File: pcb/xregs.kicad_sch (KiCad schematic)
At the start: 13 parts

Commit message: WIP schematic
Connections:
- net XD.0: now reaches U?.10 (Q5)
- net XE.0: now reaches U?.11 (Q6)
- net XF.0: now reaches U?.12 (Q7)
- net X8.0: now reaches U?.4 (Q0)
- net X9.0: now reaches U?.5 (Q1)
- net XA.0: now reaches U?.6 (Q2)
- net XB.0: now reaches U?.7 (Q3)
- net XC.0: now reaches U?.9 (Q4)
- net XD.1: now reaches U?.10 (Q5)
- net XE.1: now reaches U?.11 (Q6)
- net XF.1: now reaches U?.12 (Q7)
- net X8.1: now reaches U?.4 (Q0)
- net X9.1: now reaches U?.5 (Q1)
- net XA.1: now reaches U?.6 (Q2)
- net XB.1: now reaches U?.7 (Q3)
- net XC.1: now reaches U?.9 (Q4)

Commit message: WIP schematic
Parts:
- gave numbers to parts that had none: 9
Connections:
- net VCC renamed +5V

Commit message: WIP PCB
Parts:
- renumbered U42 to U?, U46 to U?, U50 to U?, U48 to U?, U47 to U?, U44 to U?, U43 to U?, U45 to U?, U49 to U?
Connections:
- net XD.2: now reaches U?.10 (Q5)
- net XE.2: now reaches U?.11 (Q6)
- net XF.2: now reaches U?.12 (Q7)
- net X8.2: now reaches U?.4 (Q0)
- net X9.2: now reaches U?.5 (Q1)
- net XA.2: now reaches U?.6 (Q2)
- net XB.2: now reaches U?.7 (Q3)
- net XC.2: now reaches U?.9 (Q4)
- net XD.3: now reaches U?.10 (Q5)
- net XE.3: now reaches U?.11 (Q6)
- net XF.3: now reaches U?.12 (Q7)
- net X8.3: now reaches U?.4 (Q0)
- net X9.3: now reaches U?.5 (Q1)
- net XA.3: now reaches U?.6 (Q2)
- net XB.3: now reaches U?.7 (Q3)
- net XC.3: now reaches U?.9 (Q4)

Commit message: PCB: add reset circuit, xtal
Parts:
- gave numbers to parts that had none: 10

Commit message: WIP schematic
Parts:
- renumbered U47 to U48, U48 to U49, U49 to U50, U50 to U51, U51 to U52, U52 to U53, U53 to U54, U54 to U55, U55 to U56, U5 to U6

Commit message: WIP schematic
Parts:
- renumbered U6 to U7
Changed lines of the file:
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@@
 		(dnp no)
 		(fields_autoplaced yes)
-		(property "Reference" "U6"
+		(property "Reference" "U7"
 			(at 62.23 120.6499 0)
 			(effects
@@
 			(project ""
 				(path "/e63e39d7-6ac0-4ffd-8aa3-1841a4541b55/ec11039d-e120-4fa7-aaf4-831995f0a346"
-					(reference "U6")
+					(reference "U7")
 					(unit 5)
 				)

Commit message: WIP schematic
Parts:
- renumbered U7 to U48
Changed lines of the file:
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@@
 		(dnp no)
 		(fields_autoplaced yes)
-		(property "Reference" "#PWR0191"
+		(property "Reference" "#PWR0208"
 			(at 147.32 74.93 0)
 			(effects
@@
 			(project ""
 				(path "/e63e39d7-6ac0-4ffd-8aa3-1841a4541b55/ec11039d-e120-4fa7-aaf4-831995f0a346"
-					(reference "#PWR0191")
+					(reference "#PWR0208")
 					(unit 1)
 				)
@@
 		(dnp no)
 		(fields_autoplaced yes)
-		(property "Reference" "#PWR0195"
+		(property "Reference" "#PWR0212"
 			(at 198.12 74.93 0)
 			(effects
@@
 			(project "fnx51"
 				(path "/e63e39d7-6ac0-4ffd-8aa3-1841a4541b55/ec11039d-e120-4fa7-aaf4-831995f0a346"
-					(reference "#PWR0195")
+					(reference "#PWR0212")
 					(unit 1)
 				)
@@
 		(dnp no)
 		(fields_autoplaced yes)
-		(property "Reference" "#PWR0193"
+		(property "Reference" "#PWR0210"
 			(at 147.32 151.13 0)
 			(effects
@@
 			(project "fnx51"
 				(path "/e63e39d7-6ac0-4ffd-8aa3-1841a4541b55/ec11039d-e120-4fa7-aaf4-831995f0a346"
-					(reference "#PWR0193")
+					(reference "#PWR0210")
 					(unit 1)
 				)
@@
 		(dnp no)
 		(fields_autoplaced yes)
-		(property "Reference" "#PWR0185"
+		(property "Reference" "#PWR0202"
 			(at 55.88 140.97 0)
 			(effects
@@
 			(project ""
 				(path "/e63e39d7-6ac0-4ffd-8aa3-1841a4541b55/ec11039d-e120-4fa7-aaf4-831995f0a346"
-					(reference "#PWR0185")
+					(reference "#PWR0202")
 					(unit 1)
 				)
@@
 		(dnp no)
 		(fields_autoplaced yes)
-		(property "Reference" "#PWR0199"
+		(property "Reference" "#PWR0216"
 			(at 248.92 74.93 0)
 			(effects
@@
 			(project "fnx51"
 				(path "/e63e39d7-6ac0-4ffd-8aa3-1841a4541b55/ec11039d-e120-4fa7-aaf4-831995f0a346"
-					(reference "#PWR0199")
+					(reference "#PWR0216")
 					(unit 1)
 				)
@@
 		(on_board yes)
 		(dnp no)
-		(property "Reference" "#PWR0194"
+		(property "Reference" "#PWR0211"
 			(at 198.12 36.83 0)
 			(effects
@@
 			(project "fnx51"
 				(path "/e63e39d7-6ac0-4ffd-8aa3-1841a4541b55/ec11039d-e120-4fa7-aaf4-831995f0a346"
-					(reference "#PWR0194")
+					(reference "#PWR0211")
 					(unit 1)
 				)
@@
 		(on_board yes)
 		(dnp no)
-		(property "Reference" "#PWR0192"
+		(property "Reference" "#PWR0209"
 			(at 147.32 113.03 0)
 			(effects
@@
 			(project "fnx51"
 				(path "/e63e39d7-6ac0-4ffd-8aa3-1841a4541b55/ec11039d-e120-4fa7-aaf4-831995f0a346"
-					(reference "#PWR0192")
+					(reference "#PWR0209")
 					(unit 1)
 				)
@@
 		(dnp no)
 		(fields_autoplaced yes)
-		(property "Reference" "#PWR0189"
+		(property "Reference" "#PWR0206"
 			(at 96.52 151.13 0)
 			(effects
@@
 			(project "fnx51"
 				(path "/e63e39d7-6ac0-4ffd-8aa3-1841a4541b55/ec11039d-e120-4fa7-aaf4-831995f0a346"
-					(reference "#PWR0189")
+					(reference "#PWR0206")
 					(unit 1)
 				)
@@
 		(dnp no)
 		(fields_autoplaced yes)
-		(property "Reference" "#PWR0187"
+		(property "Reference" "#PWR0204"
 			(at 96.52 74.93 0)
 			(effects
@@
 			(project "fnx51"
 				(path "/e63e39d7-6ac0-4ffd-8aa3-1841a4541b55/ec11039d-e120-4fa7-aaf4-831995f0a346"
-					(reference "#PWR0187")
+					(reference "#PWR0204")
 					(unit 1)
 				)
@@
 		(on_board yes)
 		(dnp no)
-		(property "Reference" "#PWR0200"
+		(property "Reference" "#PWR0217"
 			(at 248.92 113.03 0)
 			(effects
@@
 			(project "fnx51"
 				(path "/e63e39d7-6ac0-4ffd-8aa3-1841a4541b55/ec11039d-e120-4fa7-aaf4-831995f0a346"
-					(reference "#PWR0200")
+					(reference "#PWR0217")
 					(unit 1)
 				)
@@
 		(dnp no)
 		(fields_autoplaced yes)
-		(property "Reference" "#PWR0197"
+		(property "Reference" "#PWR0214"
 			(at 198.12 151.13 0)
 			(effects
@@
 			(project "fnx51"
 				(path "/e63e39d7-6ac0-4ffd-8aa3-1841a4541b55/ec11039d-e120-4fa7-aaf4-831995f0a346"
-					(reference "#PWR0197")
+					(reference "#PWR0214")
 					(unit 1)
 				)
@@
 		(on_board yes)
 		(dnp no)
-		(property "Reference" "#PWR0190"
+		(property "Reference" "#PWR0207"
 			(at 147.32 36.83 0)
 			(effects
@@
 			(project ""
 				(path "/e63e39d7-6ac0-4ffd-8aa3-1841a4541b55/ec11039d-e120-4fa7-aaf4-831995f0a346"
-					(reference "#PWR0190")
+					(reference "#PWR0207")
 					(unit 1)
 				)
@@
 		(dnp no)
 		(fields_autoplaced yes)
-		(property "Reference" "#PWR0201"
+		(property "Reference" "#PWR0218"
 			(at 248.92 151.13 0)
 			(effects
@@
 			(project "fnx51"
 				(path "/e63e39d7-6ac0-4ffd-8aa3-1841a4541b55/ec11039d-e120-4fa7-aaf4-831995f0a346"
-					(reference "#PWR0201")
+					(reference "#PWR0218")
 					(unit 1)
 				)
@@
 		(dnp no)
 		(fields_autoplaced yes)
-		(property "Reference" "#PWR0184"
+		(property "Reference" "#PWR0201"
 			(at 55.88 113.03 0)
 			(effects
@@
 			(project ""
 				(path "/e63e39d7-6ac0-4ffd-8aa3-1841a4541b55/ec11039d-e120-4fa7-aaf4-831995f0a346"
-					(reference "#PWR0184")
+					(reference "#PWR0201")
 					(unit 1)
 				)
@@
 		(on_board yes)
 		(dnp no)
-		(property "Reference" "#PWR0198"
+		(property "Reference" "#PWR0215"
 			(at 248.92 36.83 0)
 			(effects
@@
 			(project "fnx51"
 				(path "/e63e39d7-6ac0-4ffd-8aa3-1841a4541b55/ec11039d-e120-4fa7-aaf4-831995f0a346"
-					(reference "#PWR0198")
+					(reference "#PWR0215")
 					(unit 1)
 				)
@@
 		(on_board yes)
 		(dnp no)
-		(property "Reference" "#PWR0196"
+		(property "Reference" "#PWR0213"
 			(at 198.12 113.03 0)
 			(effects
@@
 			(project "fnx51"
 				(path "/e63e39d7-6ac0-4ffd-8aa3-1841a4541b55/ec11039d-e120-4fa7-aaf4-831995f0a346"
-					(reference "#PWR0196")
+					(reference "#PWR0213")
 					(unit 1)
 				)
@@
 		(dnp no)
 		(fields_autoplaced yes)
-		(property "Reference" "U7"
+		(property "Reference" "U48"
 			(at 62.23 120.6499 0)
 			(effects
@@
 			(project ""
 				(path "/e63e39d7-6ac0-4ffd-8aa3-1841a4541b55/ec11039d-e120-4fa7-aaf4-831995f0a346"
-					(reference "U7")
+					(reference "U48")
 					(unit 5)
 				)
@@
 		(on_board yes)
 		(dnp no)
-		(property "Reference" "#PWR0186"
+		(property "Reference" "#PWR0203"
 			(at 96.52 36.83 0)
 			(effects
@@
 			(project "fnx51"
 				(path "/e63e39d7-6ac0-4ffd-8aa3-1841a4541b55/ec11039d-e120-4fa7-aaf4-831995f0a346"
-					(reference "#PWR0186")
+					(reference "#PWR0203")
 					(unit 1)
 				)
@@
 		(on_board yes)
 		(dnp no)
-		(property "Reference" "#PWR0188"
+		(property "Reference" "#PWR0205"
 			(at 96.52 113.03 0)
 			(effects
@@
 			(project "fnx51"
 				(path "/e63e39d7-6ac0-4ffd-8aa3-1841a4541b55/ec11039d-e120-4fa7-aaf4-831995f0a346"
-					(reference "#PWR0188")
-					(unit 1)
-				)
+					(reference "#PWR0205")
+					(unit 1)
+				)

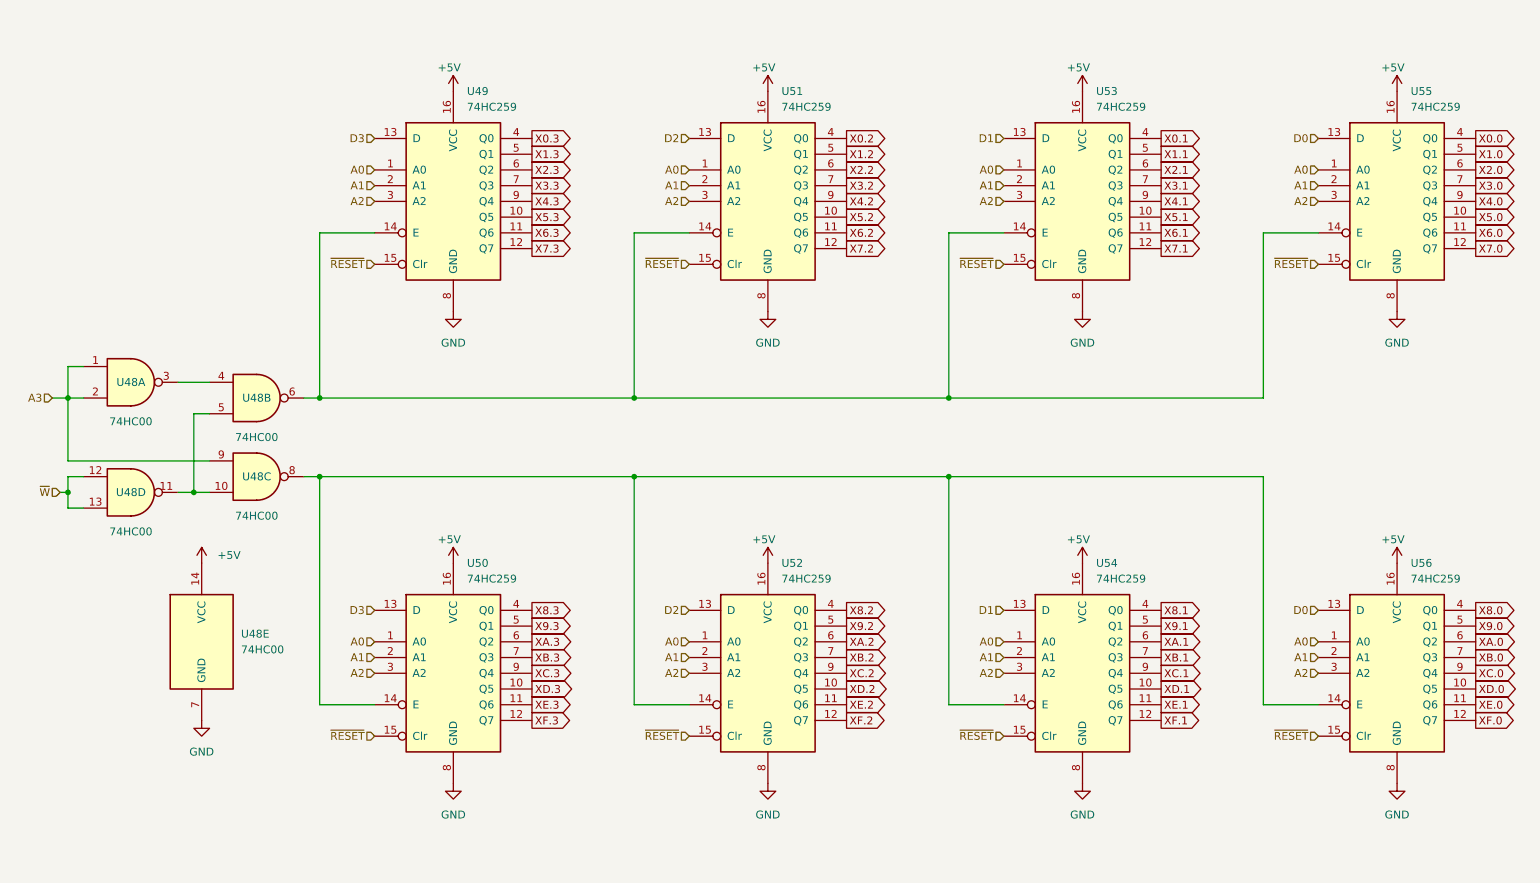
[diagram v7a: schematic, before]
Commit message: WIP PCB (add bypass caps, minor fixes)
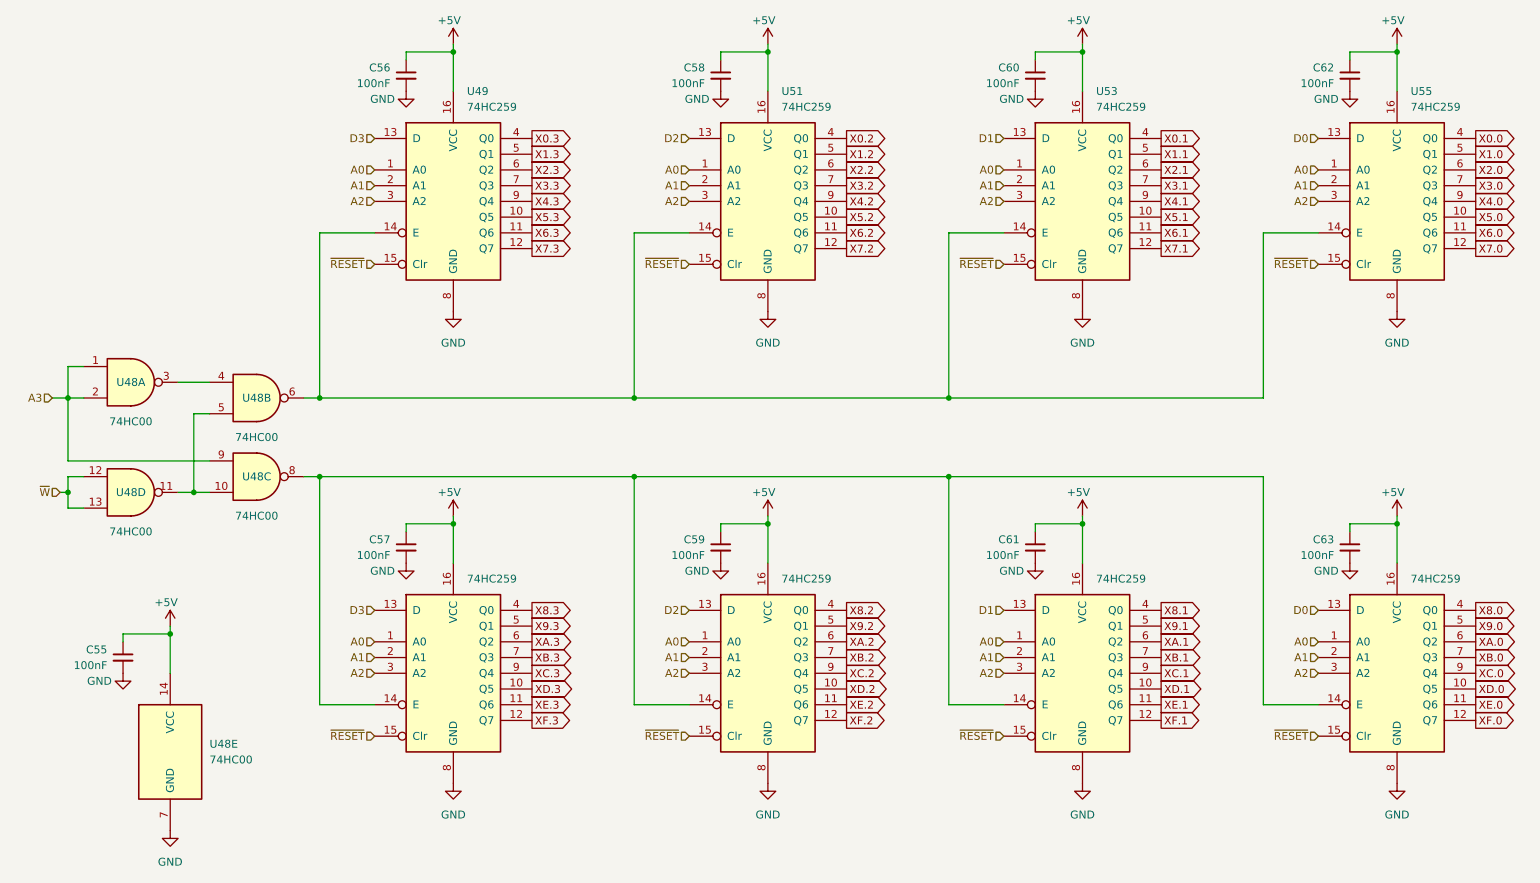
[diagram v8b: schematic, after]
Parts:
- added C55, C56, C57, C58, C59, C60, C61, C62, C63: 100nF, symbol Device:C_Small
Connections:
- net +5V: now also C55.1, C56.1, C57.1, C58.1, C59.1, C60.1, C61.1, C62.1, C63.1
- net GND: now also C55.2, C56.2, C57.2, C58.2, C59.2, C60.2, C61.2, C62.2, C63.2
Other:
- moved on the sheet: U48E
